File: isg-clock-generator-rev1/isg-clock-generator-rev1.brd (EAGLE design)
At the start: 76.2 x 76.2 mm, 162 parts, among them IC1 LMK03318RHSR, IC4 TPS7A8001DRBR, IC5 TPS7A8001DRBR, Q1 7M50072001, X1 OUT2_P, X2 OUT2_N, X3 OUT0_P, X4 PRIREF_P, X5 PRIREF_N, X6 V_IN_EXT

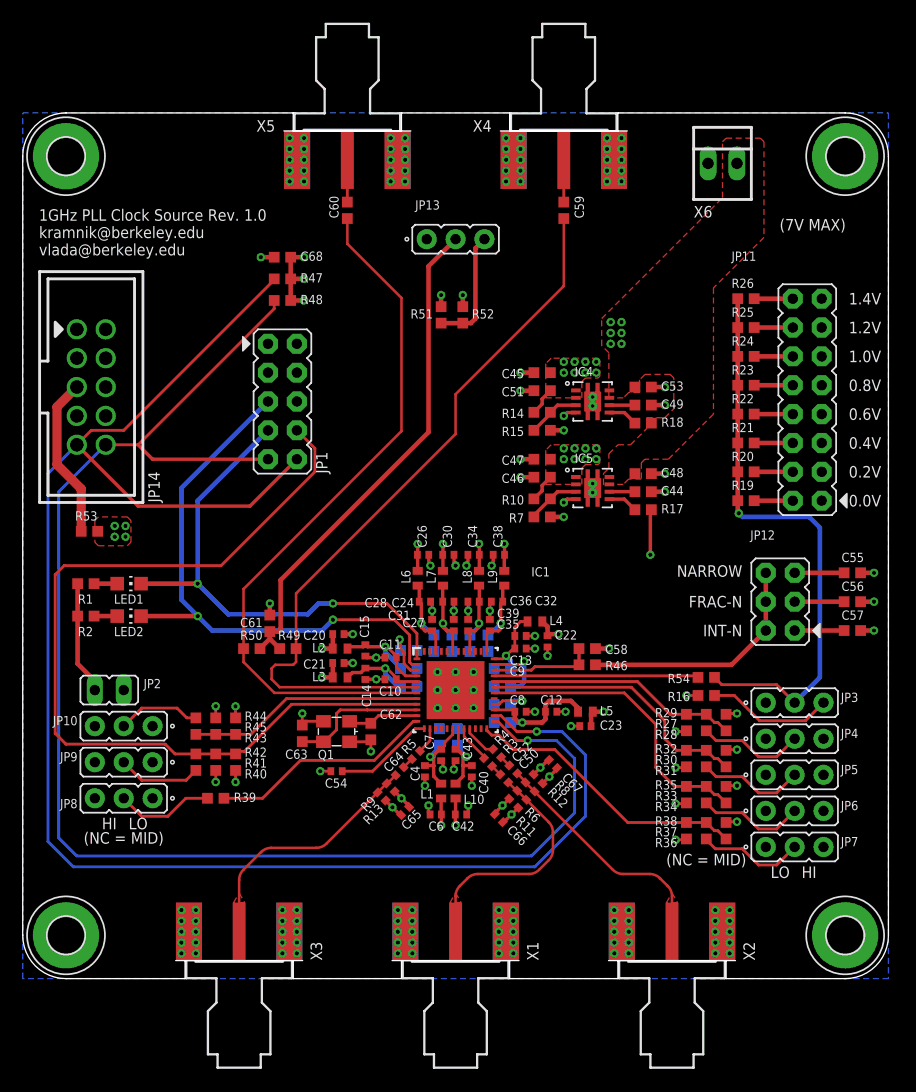
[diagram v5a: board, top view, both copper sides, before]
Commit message: BOM and centroid files for assembly quote
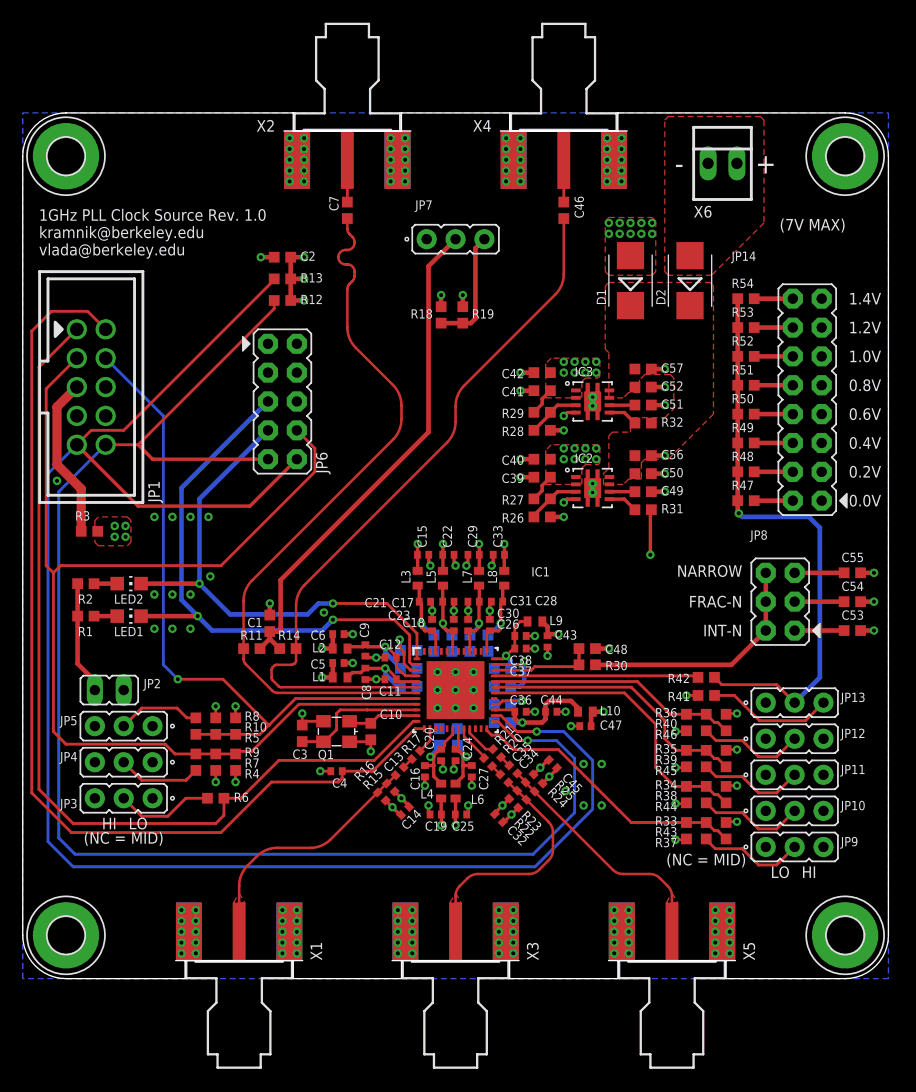
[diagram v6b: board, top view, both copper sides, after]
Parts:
- removed C58, C62, C63: DNP, rcl-modified-footprints:C0603
- removed C59, C60: 0R JUMPER, rcl-modified-footprints:C0603
- removed C61: DNP 0603, rcl-modified-footprints:C0603
- removed C64: 0R JUMPER 0402, rcl-modified-footprints:C0402
- removed C65, C66, C67: CAP CER 0.1uF X7R 0402, rcl-modified-footprints:C0402
- removed C68: CAP CER 0.1UF 25V X7R 0603 10%, rcl-modified-footprints:C0603
- added C100, C101, C102, C103, C104, C105, C106, C107, C108, C109, C110, C111, C112: CAP CER 10uF 6.3V X5R 0603, rcl-modified-footprints:C0603
- added D1, D2: SL23HE3_A/I, diode:SMB
- C1, C3: value CAP CER 10uF 6.3V X5R 0603 -> DNP
- C10: value CAP CER 0.01uF X7R 0402 -> DNP; device rcl-modified-footprints:C0402 -> rcl-modified-footprints:C0603
- C12, C20, C23, C24, C26, C30, C36, C4: value CAP CER 0.1uF X7R 0402 -> CAP CER 0.01uF X7R 0402
- C13, C34: value CAP CER 0.1uF X7R 0402 -> 0R JUMPER 0402
- C16, C17, C19, C25, C29, C33, C5: value CAP CER 10uF 6.3V X5R 0603 -> CAP CER 0.1uF X7R 0402; device rcl-modified-footprints:C0603 -> rcl-modified-footprints:C0402
- C18, C37: value CAP CER 10uF 6.3V X5R 0603 -> CAP CER 0.01uF X7R 0402; device rcl-modified-footprints:C0603 -> rcl-modified-footprints:C0402
- C2, C41: value CAP CER 10uF 6.3V X5R 0603 -> CAP CER 0.1UF 25V X7R 0603 10%
- C27, C31, C43, C8, C9: value CAP CER 0.01uF X7R 0402 -> CAP CER 0.1uF X7R 0402
- C35: value CAP CER 0.01uF X7R 0402 -> 0R JUMPER 0402
- C39: value CAP CER 0.01uF X7R 0402 -> CAP CER 0.1UF 25V X7R 0603 10%; device rcl-modified-footprints:C0402 -> rcl-modified-footprints:C0603
- C40, C42: value CAP CER 0.1uF X7R 0402 -> CAP CER 4.7UF 6.3V X5R 0603 10%; device rcl-modified-footprints:C0402 -> rcl-modified-footprints:C0603
- C44: value CAP CER 10000PF 25V X7R 0603 10% -> CAP CER 0.1uF X7R 0402; device rcl-modified-footprints:C0603 -> rcl-modified-footprints:C0402
- C45, C47: value CAP CER 4.7UF 6.3V X5R 0603 10% -> CAP CER 0.1uF X7R 0402; device rcl-modified-footprints:C0603 -> rcl-modified-footprints:C0402
- C46: value CAP CER 0.1UF 25V X7R 0603 10% -> 0R JUMPER 0603
- C48: value CAP CER 0.1UF 25V X7R 0603 10% -> DNP
- C50, C52: value 0R JUMPER 0402 -> CAP CER 0.1UF 25V X7R 0603 10%; device rcl-modified-footprints:C0402 -> rcl-modified-footprints:C0603
- C51: value CAP CER 0.1UF 25V X7R 0603 10% -> CAP CER 10000PF 25V X7R 0603 10%
- C53: value CAP CER 0.1UF 25V X7R 0603 10% -> CAP CER 3300pF X7R 0603
- C54: value CAP CER 0.01uF X7R 0402 -> CAP CER 0.033uF X7R 0603; device rcl-modified-footprints:C0402 -> rcl-modified-footprints:C0603
- C56: value CAP CER 0.033uF 0603 -> CAP CER 1UF 10V X7R 0603 10%
- C57: value CAP CER 3300pF 0603 -> CAP CER 1UF 10V X7R 0603 10%
- C7: value CAP CER 0.01uF X7R 0402 -> 0R JUMPER 0603; device rcl-modified-footprints:C0402 -> rcl-modified-footprints:C0603
- JP1: value EOS_MOTHERBOARD -> TI_USB2ANY; device isg-clock-generator:JP5Q -> Kramnik's Library:CON_OST_302-S101
- JP10: value REFSEL -> GPIO2
- JP11: value XO_MARGIN -> GPIO3; device isg-clock-generator:JP8Q -> isg-clock-generator:JP2_ROUND
- JP12: value LOOP_FILTER -> GPIO4; device isg-clock-generator:JP3Q -> isg-clock-generator:JP2_ROUND
- JP13: value PRIREF_VCM -> GPIO5
- JP14: value TI_USB2ANY -> XO_MARGIN; device Kramnik's Library:CON_OST_302-S101 -> isg-clock-generator:JP8Q
- JP3: value GPIO5 -> GPIO0
- JP4: value GPIO4 -> HWCTRL
- JP5: value GPIO3 -> REFSEL
- JP6: value GPIO2 -> EOS_MOTHERBOARD; device isg-clock-generator:JP2_ROUND -> isg-clock-generator:JP5Q
- JP7: value GPIO1 -> PRIREF_VCM
- JP8: value GPIO0 -> LOOP_FILTER; device isg-clock-generator:JP2_ROUND -> isg-clock-generator:JP3Q
- JP9: value HWCTRL -> GPIO1
- LED1: value STAT0=LO -> STAT1=LO
- LED2: value STAT1=LO -> STAT0=LO
- R1, R2: value RES SMD 510R 0603 -> RES SMD 510 OHM 1% 1/10W 0603
- R10, R14, R18: value RES SMD 4.99K OHM 1% 1/10W 0603 -> DNP
- R11, R8, R9: device rcl-modified-footprints:R0402 -> rcl-modified-footprints:R0603
- R12, R13: value DNP -> RES SMD 10K OHM 1% 1/10W 0603; device rcl-modified-footprints:R0402 -> rcl-modified-footprints:R0603
- R15: value RES SMD 1.62K OHM 1% 1/10W 0603 -> DNP; device rcl-modified-footprints:R0603 -> rcl-modified-footprints:R0402
- R16: value RES SMD 1K OHM 1% 1/10W 0603 -> DNP; device rcl-modified-footprints:R0603 -> rcl-modified-footprints:R0402
- R17: value RES SMD 4.99K OHM 1% 1/10W 0603 -> 0R JUMPER 0402; device rcl-modified-footprints:R0603 -> rcl-modified-footprints:R0402
- R19: value RES SMD 0 OHM 1% 1/10W 0603 -> DNP
- R20: value RES SMD 2.32K OHM 1% 1/10W 0603 -> 0R JUMPER 0402; device rcl-modified-footprints:R0603 -> rcl-modified-footprints:R0402
- R21: value RES SMD 5.62K OHM 1% 1/10W 0603 -> 0R JUMPER 0402; device rcl-modified-footprints:R0603 -> rcl-modified-footprints:R0402
- R22: value RES SMD 10.5K OHM 1% 1/10W 0603 -> DNP; device rcl-modified-footprints:R0603 -> rcl-modified-footprints:R0402
- R23: value RES SMD 18.7K OHM 1% 1/10W 0603 -> DNP; device rcl-modified-footprints:R0603 -> rcl-modified-footprints:R0402
- R24: value RES SMD 34.8K OHM 1% 1/10W 0603 -> DNP; device rcl-modified-footprints:R0603 -> rcl-modified-footprints:R0402
- R25: value RES SMD 84.5K OHM 1% 1/10W 0603 -> DNP; device rcl-modified-footprints:R0603 -> rcl-modified-footprints:R0402
- R26: value DNP -> RES SMD 3.92K OHM 1% 1/10W 0603
- R27, R33: value RES SMD 1K OHM 1% 1/10W 0603 -> RES SMD 4.99K OHM 1% 1/10W 0603
- R28: value DNP -> RES SMD 1.62K OHM 1% 1/10W 0603
- R29: value DNP -> RES SMD 4.99K OHM 1% 1/10W 0603
- R3: value 0R JUMPER 0402 -> DNP; device rcl-modified-footprints:R0402 -> rcl-modified-footprints:R0603
- R30: value RES SMD 1K OHM 1% 1/10W 0603 -> 0R JUMPER 0603
- R31, R34: value RES SMD 13.0K OHM 1% 1/10W 0603 -> RES SMD 4.99K OHM 1% 1/10W 0603
- R36: value RES SMD 1K OHM 1% 1/10W 0603 -> DNP
- R37, R39: value RES SMD 13.0K OHM 1% 1/10W 0603 -> RES SMD 1K OHM 1% 1/10W 0603
- R38: value RES SMD 4.99K OHM 1% 1/10W 0603 -> RES SMD 1K OHM 1% 1/10W 0603
- R4: value 0R JUMPER 0402 -> RES SMD 10K OHM 1% 1/10W 0603; device rcl-modified-footprints:R0402 -> rcl-modified-footprints:R0603
- R40: value RES SMD 10K OHM 1% 1/10W 0603 -> RES SMD 1K OHM 1% 1/10W 0603
- R41: value DNP -> RES SMD 1K OHM 1% 1/10W 0603
- R42: value DNP -> 0R JUMPER 0603
- R43: value RES SMD 1K OHM 1% 1/10W 0603 -> RES SMD 13.0K OHM 1% 1/10W 0603
- R44, R45: value DNP -> RES SMD 13.0K OHM 1% 1/10W 0603
- R46, R54: value 0R JUMPER 0603 -> DNP
- R47: value RES SMD 1K OHM 1% 1/10W 0603 -> RES SMD 0 OHM 1% 1/10W 0603
- R48: value RES SMD 1K OHM 1% 1/10W 0603 -> RES SMD 2.32K OHM 1% 1/10W 0603
- R49: value DNP -> RES SMD 5.62K OHM 1% 1/10W 0603
- R5: value 0R JUMPER 0402 -> RES SMD 1K OHM 1% 1/10W 0603; device rcl-modified-footprints:R0402 -> rcl-modified-footprints:R0603
- R50: value DNP -> RES SMD 10.5K OHM 1% 1/10W 0603
- R51: value DNP 0603 -> RES SMD 18.7K OHM 1% 1/10W 0603
- R52: value DNP 0603 -> RES SMD 34.8K OHM 1% 1/10W 0603
- R53: value DNP -> RES SMD 84.5K OHM 1% 1/10W 0603
- R6: value DNP -> RES SMD 13.0K OHM 1% 1/10W 0603; device rcl-modified-footprints:R0402 -> rcl-modified-footprints:R0603
- R7: value RES SMD 3.92K OHM 1% 1/10W 0603 -> DNP
- X1: value OUT2_P -> OUT0_P
- X2: value OUT2_N -> PRIREF_N
- X3: value OUT0_P -> OUT2_P
- X5: value PRIREF_N -> OUT2_N
- moved H2 97.0 mm to (3.81, 72.4)
- moved X2 78.4 mm to (28.6, 74.6), turned to 270 degrees
- moved X5 78.4 mm to (57.1, 1.59), turned to 90 degrees
- moved H3 68.6 mm to (72.4, 3.81)
- moved H4 68.6 mm to (72.4, 72.4)
- moved JP14 63.0 mm to (69.1, 51.0), turned to 90 degrees
- moved JP7 61.3 mm to (38.1, 65.1)
- moved R53 60.5 mm to (63.7, 57.3)
- moved JP8 60.3 mm to (66.7, 33.2), turned to 90 degrees
- moved JP3 59.7 mm to (8.89, 15.9), turned to 180 degrees
- moved JP10 59.5 mm to (67.9, 14.8), turned to 0 degrees
- moved JP9 59.5 mm to (67.9, 11.6), turned to 0 degrees
- moved JP5 59.2 mm to (8.89, 22.2), turned to 180 degrees
- moved JP4 59.1 mm to (8.89, 19.1), turned to 180 degrees
- moved JP6 57.7 mm to (22.9, 50.8), turned to 270 degrees
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- renumbered IC4 to IC3, IC5 to IC2
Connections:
- removed net GPIO0: IC1.12, R39.2
- removed net N$10: JP14.3
- removed net N$11: JP14.1
- removed net N$12: JP14.8
- removed net N$13: JP14.4
- removed net N$14: JP14.2
- removed net N$9: JP14.7
- new net GPIO0/SYNC: IC1.12, JP1.1, R6.2
- new net NC_USB2ANY_CONN_1: JP1.7
- new net NC_USB2ANY_CONN_2: JP1.8
- new net VIN_EXT: D2.A, X6.2
- new net VIN_MLB: D1.A, JP6.1, JP6.2
- net DECAP_DIG: now also C102.1; no longer C1.1
- net DECAP_LDO: now also C110.1; no longer C3.1
- net DECAP_PLL: now also C111.1; no longer C2.1
- net EXT_VDD: now also JP1.5, R3.1; no longer JP14.5, R53.1
- net GND: now also C100.2, C101.2, C102.2, C103.2, C104.2, C105.2, C106.2, C107.2, C108.2, C109.2, C110.2, C111.2, C112.2, C50.2, C52.2, JP12.1, JP14.1, JP14.11, JP14.13, JP14.15, JP14.3, JP14.5, JP14.7, JP14.9, JP6.3, JP6.4, JP6.6, R10.1, R16.1, R19.1, R22.1, R24.1, R26.2, R28.2, R33.1, R34.1, R36.1, R9.1; no longer C13.2, C34.2, C35.2, C46.2, C58.2, C61.2, C62.2, C63.2, C65.2, C66.2, C67.2, C68.2, C7.2, JP1.3, JP1.4, JP11.11, JP11.13, JP11.15, JP11.3, JP11.5, JP11.7, JP11.9, JP14.6, JP6.1, JP8.1, R11.1, R12.1, R13.1, R15.2, R29.1, R32.1, R38.1, R42.1, R45.1, R52.1, R7.2
- net GPIO0_JUMPER: now also JP3.2, R6.1; no longer JP8.2, R39.1
- net GPIO1: now also R33.2, R37.2, R43.1; no longer R36.2, R37.1, R38.2
- net GPIO1_JUMPER: now also JP9.2, R37.1; no longer JP7.2, R36.1
- net GPIO2: now also R34.2, R38.2, R44.1; no longer R33.2, R34.1, R35.2
- net GPIO2_JUMPER: now also JP10.2, R38.1; no longer JP6.2, R33.1
- net GPIO3: now also R35.2, R39.2, R45.1; no longer R30.2, R31.1, R32.2
- net GPIO3_JUMPER: now also JP11.2, R39.1; no longer JP5.2, R30.1
- net GPIO4: now also R36.2, R40.2, R46.1; no longer R27.2, R28.1, R29.2
- net GPIO4_JUMPER: now also JP12.2, R40.1; no longer JP4.2, R27.1
- net GPIO5: now also R42.1; no longer R54.1
- net GPIO5_JUMPER: now also JP13.2, R42.2, R47.1, R48.1, R49.1, R50.1, R51.1, R52.1, R53.1, R54.1; no longer JP3.2, R19.1, R20.1, R21.1, R22.1, R23.1, R24.1, R25.1, R26.1, R54.2
- net GPIO5_SEL_11_12: now also JP14.12, R52.2; no longer JP11.12, R24.2
- net GPIO5_SEL_13_14: now also JP14.14, R53.2; no longer JP11.14, R25.2
- net GPIO5_SEL_15_16: now also JP14.16, R54.2; no longer JP11.16, R26.2
- net GPIO5_SEL_1_2: now also JP14.2, R47.2; no longer JP11.2, R19.2
- net GPIO5_SEL_3_4: now also JP14.4, R48.2; no longer JP11.4, R20.2
- net GPIO5_SEL_5_6: now also JP14.6, R49.2; no longer JP11.6, R21.2
- net GPIO5_SEL_7_8: now also JP14.8, R50.2; no longer JP11.8, R22.2
- net GPIO5_SEL_9_10: now also JP14.10, R51.2; no longer JP11.10, R23.2
- net HWCTRL_JUMPER: now also JP4.2, R4.1; no longer JP9.2, R40.1
- net HW_SW_CTRL: now also JP1.3, JP6.8, R4.2, R7.1, R9.2; no longer JP1.8, R40.2, R41.1, R42.2
- net LDO_PVCORE_EN: now also R32.2; no longer R18.2
- net LDO_PVCORE_FB: now also R28.1, R29.1; no longer R14.1, R15.1
- net LDO_PVCORE_SS: now also C51.1; no longer C49.1
- net LDO_PVDDIO_EN: now also R31.2; no longer R17.2
- net LDO_PVDDIO_FB: now also R26.1, R27.1; no longer R10.1, R7.1
- net LDO_PVDDIO_SS: now also C49.1; no longer C44.1
- net LF1: now also C48.1, R30.1; no longer C58.1, R46.1
- net LF_FRAC_N: now also C54.1, JP8.3; no longer C56.1, JP12.3
- net LF_INT_N\: now also C53.1, JP8.1; no longer C57.1, JP12.1
- net LF_NARROW: now also JP8.5; no longer JP12.5
- net LF_R: now also JP8.2, JP8.4, JP8.6, R30.2; no longer JP12.2, JP12.4, JP12.6, R46.2
- net OUT0_P: now also R17.2; no longer R5.2
- net OUT0_R_C_P: now also C13.2, R15.1, R16.2, X1.1; no longer C64.2, R13.2, R9.1, X3.1
- net OUT0_R_P: now also C13.1, R17.1; no longer C64.1, R5.1
- net OUT2_N: now also R21.2; no longer R4.2
- net OUT2_P: now also R20.2; no longer R3.2
- net OUT2_R_C_N: now also C35.2, R24.2, R25.1, X5.1; no longer C52.2, R12.2, R8.1, X2.1
- net OUT2_R_C_P: now also C34.2, R22.2, R23.1, X3.1; no longer C50.2, R11.2, R6.1, X1.1
- net OUT2_R_N: now also C35.1, R21.1; no longer C52.1, R4.1
- net OUT2_R_P: now also C34.1, R20.1; no longer C50.1, R3.1
- net PDN: now also C4.1, JP1.2; no longer C54.1
- net PP_P1V8_VDDO: now also C14.1, C15.1, C19.1, C22.1, C25.1, C29.1, C32.1, C33.1, C39.1, C40.1, C45.1, L3.2, L4.2, L5.2, R15.2, R23.2, R25.2, R27.2; no longer C26.1, C30.1, C34.1, C38.1, C42.1, C46.1, C47.1, C6.1, C65.1, C66.1, C67.1, L1.2, L10.2, L9.2, R10.2, R6.2, R8.2, R9.2
- net PP_P3V3_PLL_CORE: now also C2.1, C41.1, C42.1, C43.1, C47.1, C5.1, C6.1, JP11.3, JP12.3, JP3.3, L1.1, L10.1, L9.1, R12.2, R13.2, R18.2, R29.2, R3.2, R31.1, R43.2, R45.2, R46.2, R7.2, R8.2; no longer C20.1, C21.1, C22.1, C23.1, C45.1, C51.1, C68.1, JP6.3, JP7.3, JP8.3, L3.1, L4.1, L5.1, R14.2, R16.2, R17.1, R28.2, R31.2, R34.2, R37.2, R47.2, R48.2, R51.2, R53.2
- net PRIREF_N: now also C7.2, R11.2; no longer C60.2, R50.2
- net PRIREF_P: now also C46.2, R14.2; no longer C59.2, R49.2
- net PRIREF_R_N: now also C7.1, X2.1; no longer C60.1, X5.1
- net PRIREF_R_P: now also C46.1; no longer C59.1
- net PRIREF_VCM: now also C1.1, JP7.2, R11.1, R14.1; no longer C61.1, JP13.2, R49.1, R50.1
- net PRIREF_VCM_DIVIDER: now also JP7.3, R18.1, R19.2; no longer JP13.3, R51.1, R52.2
- net PULLUP_GPIO5: now also JP13.3, R41.1; no longer JP3.3, R16.1
- net REFSEL: now also JP1.4, R10.2, R5.2, R8.1; no longer R43.2, R44.1, R45.2
- net REFSEL_JUMPER: now also JP5.2, R5.1; no longer JP10.2, R43.1
- net SCL: now also JP1.9, JP6.10, R13.1; no longer JP1.10, JP14.9, R47.1
- net SDA: now also JP1.10, JP6.9, R12.1; no longer JP1.9, JP14.10, R48.1
- net SECREF_N: now also C10.1; no longer C62.1
- net SECREF_P: now also C3.1; no longer C63.1
- net STATUS0: now also JP6.7, LED2.C; no longer JP1.7, LED1.C
- net STATUS1: now also JP6.5, LED1.C; no longer JP1.5, LED2.C
- net VDDO_01: now also C104.1, C16.1, C20.1, L4.1; no longer C4.1, C5.1, C7.1, L1.1
- net VDDO_23: now also C106.1, C24.1, C27.1, L6.1; no longer C40.1, C41.1, C43.1, L10.1
- net VDDO_4: now also C108.1, C30.1, C31.1, L8.1; no longer C36.1, C37.1, C39.1, L9.1
- net VDDO_5: now also C107.1, C26.1, C28.1, L7.1; no longer C32.1, C33.1, C35.1, L8.1
- net VDDO_6: now also C105.1, C21.1, C23.1, L5.1; no longer C28.1, C29.1, C31.1, L7.1
- net VDDO_7: now also C103.1, C17.1, C18.1, L3.1; no longer C24.1, C25.1, C27.1, L6.1
- net VDD_DIG: now also C101.1, C12.1, C9.1; no longer C11.1, C15.1, C16.1
- net VDD_IN: now also C100.1, C11.1, C8.1, L1.2; no longer C10.1, C14.1, C17.1, L3.2
- net VDD_LDO: now also C109.1, C36.1, C44.1, L10.2; no longer C12.1, C19.1, C8.1, L5.2
- net VDD_PLL: now also C112.1, C37.1, C38.1, L9.2; no longer C13.1, C18.1, C9.1, L4.2
- net VIN: now also C50.1, C52.1, C56.1, C57.1, D1.C, D2.C, R32.1; no longer C48.1, C53.1, JP1.1, JP1.2, R18.1, X6.2
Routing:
- net GPIO0/SYNC: track 0.00 -> 81.0 mm
- net PDN: track 8.78 -> 88.7 mm
- net REFSEL: track 20.8 -> 61.3 mm, vias 0 -> 1
- net HW_SW_CTRL: track 79.3 -> 99.9 mm
- net GPIO0: track 19.8 -> 0.00 mm
- net GND: track 92.0 -> 94.1 mm, vias 164 -> 184
- net PRIREF_N: track 63.2 -> 64.2 mm
- net VIN: track 0.83 -> 0.00 mm, vias 6 -> 0
- net PRIREF_P: track 65.2 -> 64.5 mm
- net SCL: track 147.7 -> 148.3 mm
- added copper zone on layer 1, net VIN_EXT
- added copper zone on layer 1, net VIN_MLB
- added copper zone on layer 15, net VIN_MLB
- removed copper zone on layer 15, net VIN
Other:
- board text added: "+"
- board text added: "-"
